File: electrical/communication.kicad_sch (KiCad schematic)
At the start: 10 parts

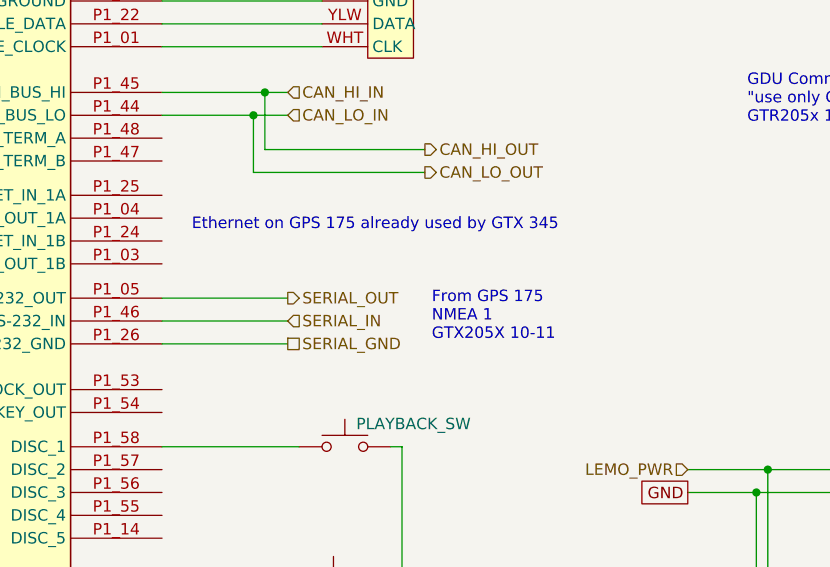
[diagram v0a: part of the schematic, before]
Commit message: Changed GPS 175 to not have connection to GTS 205x per g3xpert. Moved ELT GPS from GPS 175 and used RS-232 on GDU 460 for GEA 24 backup.
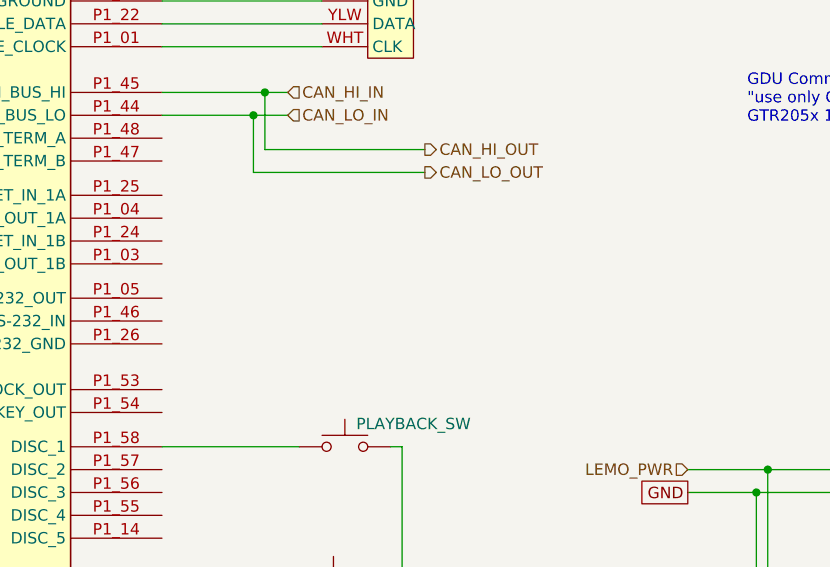
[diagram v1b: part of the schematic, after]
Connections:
- net SERIAL_GND: no longer names the net of GTR_205x.P1_26 (RS-232_GND)
- net SERIAL_IN: no longer names the net of GTR_205x.P1_46 (RS-232_IN)
- net SERIAL_OUT: no longer names the net of GTR_205x.P1_05 (RS-232_OUT)
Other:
- note removed: "Ethernet on GPS 175 already used by GTX 345"
- note removed: "From GPS 175 NMEA 1 GTX205X 10-11"
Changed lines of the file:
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@@
 	(title_block
 		(title "Communication")
-		(date "2025-09-08")
-		(rev "1.0")
+		(date "2025-09-09")
+		(rev "1.0.1")
 		(company "N78HR")
 	)
@@
 		)
 	)
-	(text "Ethernet on GPS 175 already used by GTX 345"
-		(exclude_from_sim no)
-		(at 64.262 70.612 0)
-		(effects
-			(font
-				(size 1.27 1.27)
-			)
-			(justify left)
-		)
-	)
-	(text "From GPS 175\nNMEA 1\nGTX205X 10-11"
-		(exclude_from_sim no)
-		(at 90.932 80.772 0)
-		(effects
-			(font
-				(size 1.27 1.27)
-			)
-			(justify left)
-		)
-	)
 	(junction
 		(at 165.1 139.7)
@@
 	(wire
 		(pts
-			(xy 60.96 78.74) (xy 74.93 78.74)
-		)
-		(stroke
-			(width 0)
-			(type default)
-		)
-	)
-	(wire
-		(pts
 			(xy 86.36 175.26) (xy 86.36 177.8)
 		)
@@
 	(wire
 		(pts
-			(xy 60.96 81.28) (xy 74.93 81.28)
-		)
-		(stroke
-			(width 0)
-			(type default)
-		)
-	)
-	(wire
-		(pts
 			(xy 87.63 176.53) (xy 85.09 176.53)
 		)
@@
 		(pts
 			(xy 95.25 185.42) (xy 95.25 190.5)
-		)
-		(stroke
-			(width 0)
-			(type default)
-		)
-	)
-	(wire
-		(pts
-			(xy 60.96 83.82) (xy 74.93 83.82)
 		)
 		(stroke
@@
 		)
 	)
-	(hierarchical_label "SERIAL_OUT"
-		(shape output)
-		(at 74.93 78.74 0)
-		(effects
-			(font
-				(size 1.27 1.27)
-			)
-			(justify left)
-		)
-	)
 	(hierarchical_label "CAN_HI_IN"
 		(shape input)
@@
 		)
 	)
-	(hierarchical_label "SERIAL_IN"
-		(shape input)
-		(at 74.93 81.28 0)
-		(effects
-			(font
-				(size 1.27 1.27)
-			)
-			(justify left)
-		)
-	)
 	(hierarchical_label "LEMO_PWR"
 		(shape input)
@@
 		)
 	)
-	(hierarchical_label "SERIAL_GND"
-		(shape passive)
-		(at 74.93 83.82 0)
-		(effects
-			(font
-				(size 1.27 1.27)
-			)
-			(justify left)
-		)
-	)

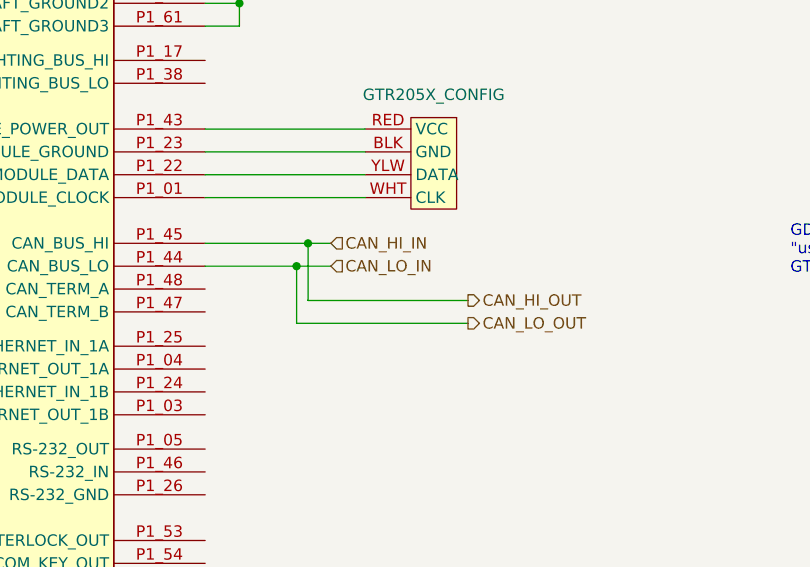
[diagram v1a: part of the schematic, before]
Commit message: Rewired canbus to match physical order.
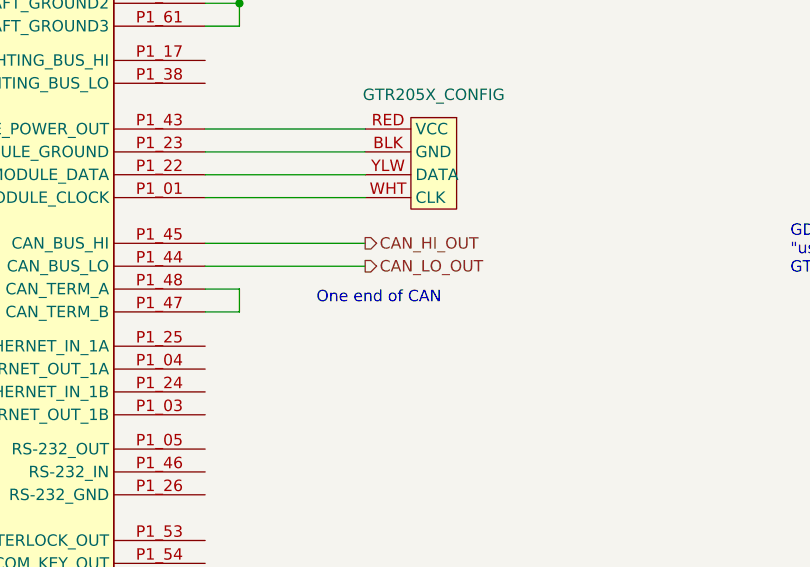
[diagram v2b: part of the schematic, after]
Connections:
- net at GTR_205x.P1_47 (CAN_TERM_B): now also GTR_205x.P1_48 (CAN_TERM_A)
- net CAN_HI_IN renamed CAN_HI_OUT
- net CAN_LO_IN renamed CAN_LO_OUT
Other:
- note added: "One end of CAN"
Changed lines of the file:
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@@
 		(title "Communication")
 		(date "2025-09-09")
-		(rev "1.0.1")
+		(rev "1.0.3")
 		(company "N78HR")
 	)
@@
 			)
 			(justify left)
+		)
+	)
+	(text "One end of CAN"
+		(exclude_from_sim no)
+		(at 80.264 61.976 0)
+		(effects
+			(font
+				(size 1.27 1.27)
+			)
 		)
 	)
@@
 	)
 	(junction
-		(at 71.12 58.42)
-		(diameter 0)
-		(color 0 0 0 0)
-	)
-	(junction
 		(at 64.77 26.67)
-		(diameter 0)
-		(color 0 0 0 0)
-	)
-	(junction
-		(at 72.39 55.88)
 		(diameter 0)
 		(color 0 0 0 0)
@@
 	(wire
 		(pts
+			(xy 64.77 60.96) (xy 64.77 63.5)
+		)
+		(stroke
+			(width 0)
+			(type default)
+		)
+	)
+	(wire
+		(pts
 			(xy 128.27 132.08) (xy 128.27 123.19)
 		)
@@
 	(wire
 		(pts
-			(xy 90.17 62.23) (xy 72.39 62.23)
+			(xy 60.96 63.5) (xy 64.77 63.5)
 		)
 		(stroke
@@
 	(wire
 		(pts
-			(xy 72.39 62.23) (xy 72.39 55.88)
-		)
-		(stroke
-			(width 0)
-			(type default)
-		)
-	)
-	(wire
-		(pts
 			(xy 60.96 115.57) (xy 111.76 115.57)
 		)
@@
 	(wire
 		(pts
-			(xy 72.39 55.88) (xy 74.93 55.88)
-		)
-		(stroke
-			(width 0)
-			(type default)
-		)
-	)
-	(wire
-		(pts
 			(xy 165.1 148.59) (xy 165.1 139.7)
 		)
@@
 	(wire
 		(pts
-			(xy 60.96 55.88) (xy 72.39 55.88)
+			(xy 60.96 60.96) (xy 64.77 60.96)
+		)
+		(stroke
+			(width 0)
+			(type default)
+		)
+	)
+	(wire
+		(pts
+			(xy 60.96 55.88) (xy 78.74 55.88)
 		)
 		(stroke
@@
 	(wire
 		(pts
-			(xy 71.12 64.77) (xy 71.12 58.42)
-		)
-		(stroke
-			(width 0)
-			(type default)
-		)
-	)
-	(wire
-		(pts
 			(xy 128.27 111.76) (xy 130.81 111.76)
 		)
@@
 	(wire
 		(pts
-			(xy 60.96 58.42) (xy 71.12 58.42)
-		)
-		(stroke
-			(width 0)
-			(type default)
-		)
-	)
-	(wire
-		(pts
-			(xy 71.12 58.42) (xy 74.93 58.42)
+			(xy 60.96 58.42) (xy 78.74 58.42)
 		)
 		(stroke
@@
 		(pts
 			(xy 60.96 129.54) (xy 109.22 129.54)
-		)
-		(stroke
-			(width 0)
-			(type default)
-		)
-	)
-	(wire
-		(pts
-			(xy 90.17 64.77) (xy 71.12 64.77)
 		)
 		(stroke
@@
 		)
 	)
-	(hierarchical_label "CAN_LO_IN"
-		(shape input)
-		(at 74.93 58.42 0)
-		(effects
-			(font
-				(size 1.27 1.27)
-			)
-			(justify left)
-		)
-	)
 	(hierarchical_label "AUDIO_IN_LO"
 		(shape input)
@@
 		)
 	)
-	(hierarchical_label "CAN_HI_IN"
-		(shape input)
-		(at 74.93 55.88 0)
-		(effects
-			(font
-				(size 1.27 1.27)
-			)
-			(justify left)
-		)
-	)
 	(hierarchical_label "CAN_HI_OUT"
 		(shape output)
-		(at 90.17 62.23 0)
+		(at 78.74 55.88 0)
 		(effects
 			(font
@@
 	(hierarchical_label "CAN_LO_OUT"
 		(shape output)
-		(at 90.17 64.77 0)
-		(effects
-			(font
+		(at 78.74 58.42 0)
+		(effects
+			(font

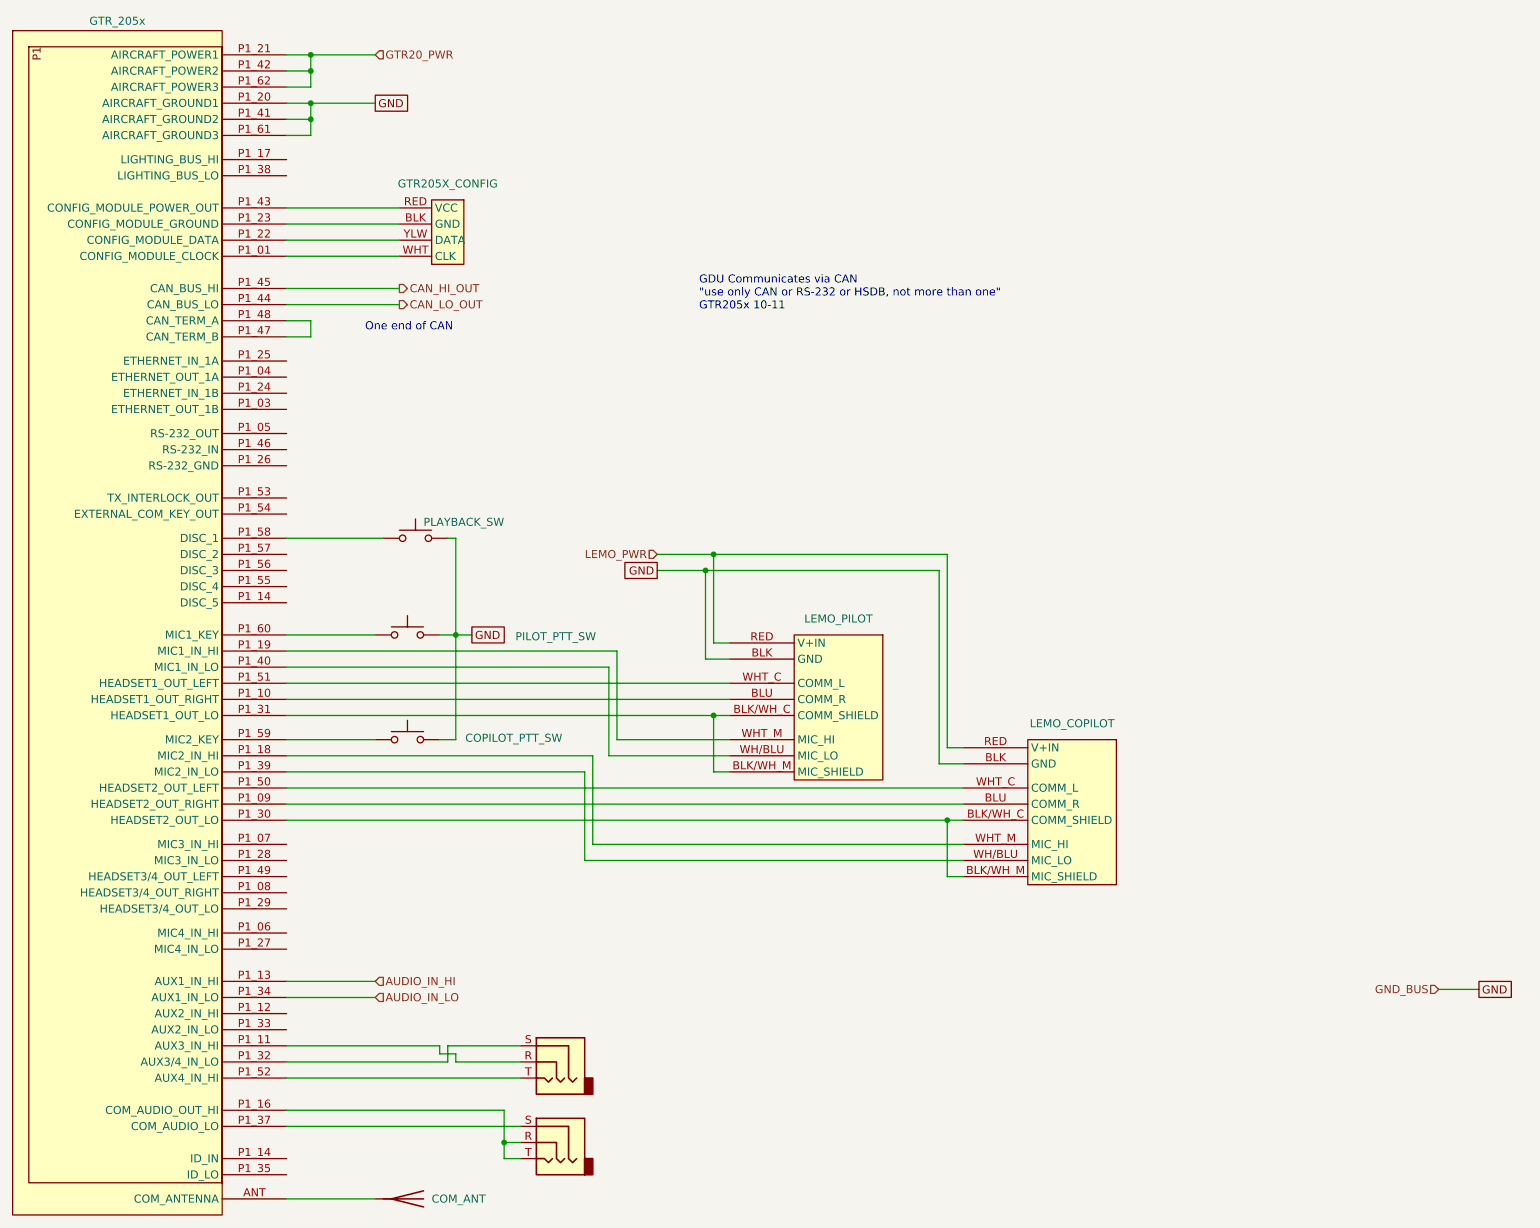
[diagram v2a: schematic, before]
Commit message: Added connectors and non-CAN/RS232/Ethernet shields.
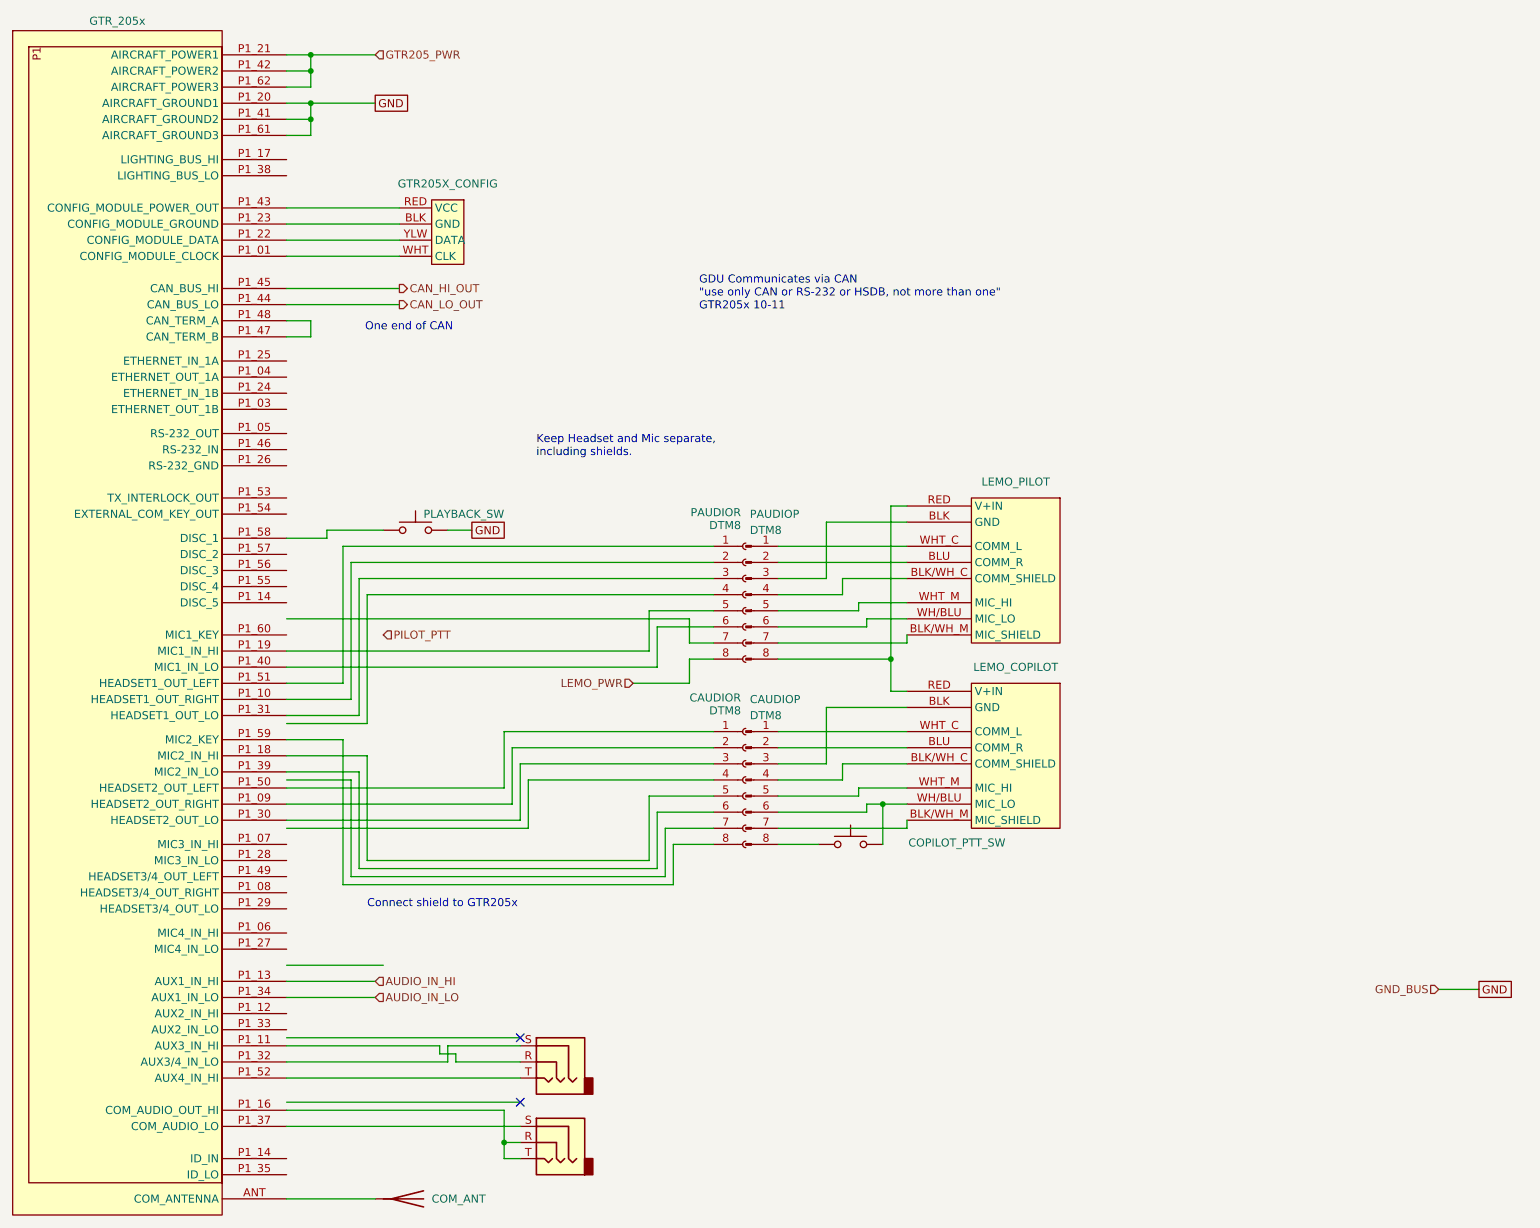
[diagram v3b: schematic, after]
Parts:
- removed PILOT_PTT_SW: SW_Push, symbol Switch:SW_Push
- added CAUDIOP, PAUDIOP: DTM8, symbol Connector:Conn_01x08_Pin
- added CAUDIOR, PAUDIOR: DTM8, symbol Connector:Conn_01x08_Socket
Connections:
- net GND: no longer COPILOT_PTT_SW.2, LEMO_COPILOT.BLK (GND), LEMO_PILOT.BLK (GND)
- net LEMO_PWR: now also PAUDIOR.8 (Pin_8); no longer LEMO_COPILOT.RED (V+IN), LEMO_PILOT.RED (V+IN)
- net at GTR_205x.P1_10 (HEADSET1_OUT_RIGHT): now also PAUDIOR.2 (Pin_2); no longer LEMO_PILOT.BLU (COMM_R)
- net at GTR_205x.P1_40 (MIC1_IN_LO): now also PAUDIOR.6 (Pin_6); no longer LEMO_PILOT.WH/BLU (MIC_LO)
- net at GTR_205x.P1_51 (HEADSET1_OUT_LEFT): now also PAUDIOR.1 (Pin_1); no longer LEMO_PILOT.WHT_C (COMM_L)
- net at GTR_205x.P1_19 (MIC1_IN_HI): now also PAUDIOR.5 (Pin_5); no longer LEMO_PILOT.WHT_M (MIC_HI)
- net at COPILOT_PTT_SW.1: now also CAUDIOP.8 (Pin_8); no longer GTR_205x.P1_59 (MIC2_KEY)
- net at LEMO_COPILOT.BLU (COMM_R): now also CAUDIOP.2 (Pin_2); no longer GTR_205x.P1_09 (HEADSET2_OUT_RIGHT)
- net at LEMO_COPILOT.WH/BLU (MIC_LO): now also COPILOT_PTT_SW.2, CAUDIOP.6 (Pin_6); no longer GTR_205x.P1_39 (MIC2_IN_LO)
- net at LEMO_COPILOT.WHT_C (COMM_L): now also CAUDIOP.1 (Pin_1); no longer GTR_205x.P1_50 (HEADSET2_OUT_LEFT)
- net at LEMO_COPILOT.WHT_M (MIC_HI): now also CAUDIOP.5 (Pin_5); no longer GTR_205x.P1_18 (MIC2_IN_HI)
- net GTR20_PWR renamed GTR205_PWR
- new net: CAUDIOP.3 (Pin_3), LEMO_COPILOT.BLK (GND)
- new net: CAUDIOP.4 (Pin_4), LEMO_COPILOT.BLK/WH_C (COMM_SHIELD)
- new net: CAUDIOP.7 (Pin_7), LEMO_COPILOT.BLK/WH_M (MIC_SHIELD)
- new net: GTR_205x.P1_31 (HEADSET1_OUT_LO), PAUDIOR.3 (Pin_3)
- new net: LEMO_PILOT.BLK (GND), PAUDIOP.3 (Pin_3)
- new net: LEMO_PILOT.BLK/WH_C (COMM_SHIELD), PAUDIOP.4 (Pin_4)
- new net: LEMO_PILOT.BLK/WH_M (MIC_SHIELD), PAUDIOP.7 (Pin_7)
- new net: LEMO_PILOT.BLU (COMM_R), PAUDIOP.2 (Pin_2)
- new net: LEMO_COPILOT.RED (V+IN), LEMO_PILOT.RED (V+IN), PAUDIOP.8 (Pin_8)
- new net: LEMO_PILOT.WH/BLU (MIC_LO), PAUDIOP.6 (Pin_6)
- new net: LEMO_PILOT.WHT_C (COMM_L), PAUDIOP.1 (Pin_1)
- new net: LEMO_PILOT.WHT_M (MIC_HI), PAUDIOP.5 (Pin_5)
- new net: CAUDIOR.1 (Pin_1), GTR_205x.P1_50 (HEADSET2_OUT_LEFT)
- new net: CAUDIOR.2 (Pin_2), GTR_205x.P1_09 (HEADSET2_OUT_RIGHT)
- new net: CAUDIOR.3 (Pin_3), GTR_205x.P1_30 (HEADSET2_OUT_LO)
- new net: CAUDIOR.5 (Pin_5), GTR_205x.P1_18 (MIC2_IN_HI)
- new net: CAUDIOR.6 (Pin_6), GTR_205x.P1_39 (MIC2_IN_LO)
- new net: CAUDIOR.8 (Pin_8), GTR_205x.P1_59 (MIC2_KEY)
- no-connect marks 0 -> 2
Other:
- note added: "Connect shield to GTR205x"
- note added: "Keep Headset and Mic separate, including shields."
- moved on the sheet: COPILOT_PTT_SW, LEMO_COPILOT, LEMO_PILOT, PLAYBACK_SW
